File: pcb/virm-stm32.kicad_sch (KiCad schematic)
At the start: 25 parts, among them J1 Conn_02x10, J2 Conn_01x04, J3 TYPE-C-31-M-12, SW1 SW_SPDT, SW2 SW_Push, SW3 SW_Push, SW4 SW_Push, U1 STM32F070CBTx, U2 XC6206P332MR, Y1 16MHz

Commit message: Added footprint for usb port
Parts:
- J3: footprint (none) -> LCSC:TYPE-C-31-M-12
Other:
- note added: "Check if SCA/SCL is not inverted"
- note added: "Maybe add battery and regulator to wear it"
- note added: "TODO check pins for tristate capabilities"
- note added: "TODO: check footprint assigned pins"
- note removed: "SCA/SCL"
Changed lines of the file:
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@@
 	)
 	(junction
-		(at 77.47 111.76)
+		(at 50.8 175.26)
 		(diameter 0)
 		(color 0 0 0 0)
 	)
 	(junction
-		(at 50.8 175.26)
+		(at 74.93 35.56)
 		(diameter 0)
 		(color 0 0 0 0)
 	)
 	(junction
-		(at 74.93 35.56)
+		(at 59.69 160.02)
 		(diameter 0)
 		(color 0 0 0 0)
 	)
 	(junction
-		(at 59.69 160.02)
+		(at 36.83 116.84)
 		(diameter 0)
 		(color 0 0 0 0)
@@
 	)
 	(junction
+		(at 74.93 111.76)
+		(diameter 0)
+		(color 0 0 0 0)
+	)
+	(junction
 		(at 36.83 45.72)
 		(diameter 0)
@@
 	)
 	(junction
-		(at 41.91 116.84)
-		(diameter 0)
-		(color 0 0 0 0)
-	)
-	(junction
 		(at 87.63 45.72)
 		(diameter 0)
@@
 	(wire
 		(pts
-			(xy 50.8 111.76) (xy 52.07 111.76)
+			(xy 45.72 111.76) (xy 52.07 111.76)
 		)
 		(stroke
@@
 	(wire
 		(pts
-			(xy 50.8 109.22) (xy 52.07 109.22)
+			(xy 45.72 109.22) (xy 52.07 109.22)
 		)
 		(stroke
@@
 	(wire
 		(pts
-			(xy 41.91 116.84) (xy 52.07 116.84)
-		)
-		(stroke
-			(width 0)
-			(type default)
-		)
-	)
-	(wire
-		(pts
 			(xy 238.76 130.81) (xy 241.3 130.81)
 		)
@@
 	(wire
 		(pts
-			(xy 41.91 116.84) (xy 41.91 123.19)
+			(xy 36.83 116.84) (xy 36.83 123.19)
 		)
 		(stroke
@@
 	(wire
 		(pts
-			(xy 50.8 104.14) (xy 52.07 104.14)
+			(xy 45.72 104.14) (xy 52.07 104.14)
 		)
 		(stroke
@@
 	(wire
 		(pts
-			(xy 64.77 111.76) (xy 77.47 111.76)
+			(xy 64.77 111.76) (xy 74.93 111.76)
 		)
 		(stroke
@@
 	(wire
 		(pts
-			(xy 41.91 106.68) (xy 52.07 106.68)
+			(xy 36.83 106.68) (xy 52.07 106.68)
 		)
 		(stroke
@@
 	(wire
 		(pts
-			(xy 77.47 101.6) (xy 77.47 111.76)
+			(xy 74.93 101.6) (xy 74.93 111.76)
 		)
 		(stroke
@@
 	(wire
 		(pts
-			(xy 64.77 101.6) (xy 77.47 101.6)
+			(xy 64.77 101.6) (xy 74.93 101.6)
 		)
 		(stroke
@@
 	(wire
 		(pts
-			(xy 41.91 106.68) (xy 41.91 116.84)
+			(xy 36.83 106.68) (xy 36.83 116.84)
 		)
 		(stroke
@@
 	(wire
 		(pts
-			(xy 50.8 119.38) (xy 52.07 119.38)
+			(xy 36.83 116.84) (xy 52.07 116.84)
+		)
+		(stroke
+			(width 0)
+			(type default)
+		)
+	)
+	(wire
+		(pts
+			(xy 45.72 119.38) (xy 52.07 119.38)
 		)
 		(stroke
@@
 	(wire
 		(pts
-			(xy 77.47 111.76) (xy 77.47 123.19)
+			(xy 74.93 111.76) (xy 74.93 123.19)
 		)
 		(stroke
@@
 	(wire
 		(pts
-			(xy 50.8 114.3) (xy 52.07 114.3)
+			(xy 45.72 114.3) (xy 52.07 114.3)
 		)
 		(stroke
@@
 	(wire
 		(pts
-			(xy 50.8 121.92) (xy 52.07 121.92)
+			(xy 45.72 121.92) (xy 52.07 121.92)
 		)
 		(stroke
@@
 		)
 	)
-	(text "SCA/SCL\n"
-		(exclude_from_sim yes)
-		(at 94.996 100.584 0)
+	(text "TODO check pins for tristate capabilities"
+		(exclude_from_sim no)
+		(at 152.4 49.784 0)
+		(effects
+			(font
+				(size 1.27 1.27)
+			)
+		)
+	)
+	(text "TODO: check footprint assigned pins"
+		(exclude_from_sim no)
+		(at 218.44 137.16 0)
+		(effects
+			(font
+				(size 1.27 1.27)
+			)
+		)
+	)
+	(text "Check if SCA/SCL is not inverted"
+		(exclude_from_sim no)
+		(at 34.29 106.426 0)
+		(effects
+			(font
+				(size 1.27 1.27)
+			)
+		)
+	)
+	(text "Maybe add battery and regulator to wear it"
+		(exclude_from_sim no)
+		(at 207.772 21.082 0)
 		(effects
 			(font
@@
 		)
 	)
+	(label "SCA"
+		(at 46.99 109.22 0)
+		(fields_autoplaced yes)
+		(effects
+			(font
+				(size 1.27 1.27)
+			)
+			(justify left bottom)
+		)
+	)
 	(label "BOOT0"
 		(at 85.09 60.96 0)
@@
 		)
 	)
+	(label "SCL"
+		(at 46.99 111.76 0)
+		(fields_autoplaced yes)
+		(effects
+			(font
+				(size 1.27 1.27)
+			)
+			(justify left bottom)
+		)
+	)
 	(global_label "LED4"
 		(shape input)
@@
 	(global_label "PB6"
 		(shape input)
-		(at 50.8 111.76 180)
+		(at 45.72 111.76 180)
 		(fields_autoplaced yes)
 		(effects
@@
 		)
 		(property "Intersheetrefs" "${INTERSHEET_REFS}"
-			(at 44.0653 111.76 0)
+			(at 38.9853 111.76 0)
 			(effects
 				(font
@@
 	(global_label "PB7"
 		(shape input)
-		(at 50.8 109.22 180)
+		(at 45.72 109.22 180)
 		(fields_autoplaced yes)
 		(effects
@@
 		)
 		(property "Intersheetrefs" "${INTERSHEET_REFS}"
-			(at 44.0653 109.22 0)
+			(at 38.9853 109.22 0)
 			(effects
 				(font
@@
 	(global_label "PB8"
 		(shape input)
-		(at 50.8 104.14 180)
+		(at 45.72 104.14 180)
 		(fields_autoplaced yes)
 		(effects
@@
 		)
 		(property "Intersheetrefs" "${INTERSHEET_REFS}"
-			(at 44.0653 104.14 0)
+			(at 38.9853 104.14 0)
 			(effects
 				(font
@@
 	(global_label "PB3"
 		(shape input)
-		(at 50.8 121.92 180)
+		(at 45.72 121.92 180)
 		(fields_autoplaced yes)
 		(effects
@@
 		)
 		(property "Intersheetrefs" "${INTERSHEET_REFS}"
-			(at 44.0653 121.92 0)
+			(at 38.9853 121.92 0)
 			(effects
 				(font
@@
 	(global_label "PB5"
 		(shape input)
-		(at 50.8 114.3 180)
+		(at 45.72 114.3 180)
 		(fields_autoplaced yes)
 		(effects
@@
 		)
 		(property "Intersheetrefs" "${INTERSHEET_REFS}"
-			(at 44.0653 114.3 0)
+			(at 38.9853 114.3 0)
 			(effects
 				(font
@@
 	(global_label "PB4"
 		(shape input)
-		(at 50.8 119.38 180)
+		(at 45.72 119.38 180)
 		(fields_autoplaced yes)
 		(effects
@@
 		)
 		(property "Intersheetrefs" "${INTERSHEET_REFS}"
-			(at 44.0653 119.38 0)
+			(at 38.9853 119.38 0)
 			(effects
 				(font
@@
 	(symbol
 		(lib_id "power:GND")
-		(at 41.91 123.19 0)
+		(at 36.83 123.19 0)
 		(unit 1)
 		(exclude_from_sim no)
@@
 		(fields_autoplaced yes)
 		(property "Reference" "#PWR02"
-			(at 41.91 129.54 0)
+			(at 36.83 129.54 0)
 			(effects
 				(font
@@
 		)
 		(property "Value" "GND"
-			(at 41.91 128.27 0)
+			(at 36.83 128.27 0)
 			(effects
 				(font
@@
 		)
 		(property "Footprint" ""
-			(at 41.91 123.19 0)
+			(at 36.83 123.19 0)
 			(effects
 				(font
@@
 		)
 		(property "Datasheet" ""
-			(at 41.91 123.19 0)
+			(at 36.83 123.19 0)
 			(effects
 				(font
@@
 		)
 		(property "Description" "Power symbol creates a global label with name \"GND\" , ground"
-			(at 41.91 123.19 0)
+			(at 36.83 123.19 0)
 			(effects
 				(font
@@
 	(symbol
 		(lib_id "power:GND")
-		(at 77.47 123.19 0)
+		(at 74.93 123.19 0)
 		(unit 1)
 		(exclude_from_sim no)
@@
 		(fields_autoplaced yes)
 		(property "Reference" "#PWR08"
-			(at 77.47 129.54 0)
+			(at 74.93 129.54 0)
 			(effects
 				(font
@@
 		)
 		(property "Value" "GND"
-			(at 77.47 128.27 0)
+			(at 74.93 128.27 0)
 			(effects
 				(font
@@
 		)
 		(property "Footprint" ""
-			(at 77.47 123.19 0)
+			(at 74.93 123.19 0)
 			(effects
 				(font
@@
 		)
 		(property "Datasheet" ""
-			(at 77.47 123.19 0)
+			(at 74.93 123.19 0)
 			(effects
 				(font
@@
 		)
 		(property "Description" "Power symbol creates a global label with name \"GND\" , ground"
-			(at 77.47 123.19 0)
+			(at 74.93 123.19 0)
 			(effects
 				(font
@@
 			)
 		)
-		(property "Footprint" ""
+		(property "Footprint" "LCSC:TYPE-C-31-M-12"
 			(at 204.47 148.59 0)
 			(effects

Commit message: Started working on PCB layout
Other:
- note added: "TODO add two more pins for 18 columns of 5 leds"
- note removed: "Check if SCA/SCL is not inverted"
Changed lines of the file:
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@@
 		)
 	)
-	(text "Check if SCA/SCL is not inverted"
+	(text "Maybe add battery and regulator to wear it"
 		(exclude_from_sim no)
-		(at 34.29 106.426 0)
+		(at 207.772 21.082 0)
 		(effects
 			(font
@@
 		)
 	)
-	(text "Maybe add battery and regulator to wear it"
+	(text "TODO add two more pins for 18 columns of 5 leds"
 		(exclude_from_sim no)
-		(at 207.772 21.082 0)
+		(at 172.466 73.66 0)
 		(effects
 			(font
@@
 		)
 	)
-	(label "SCA"
+	(label "SDA"
 		(at 46.99 109.22 0)
 		(fields_autoplaced yes)

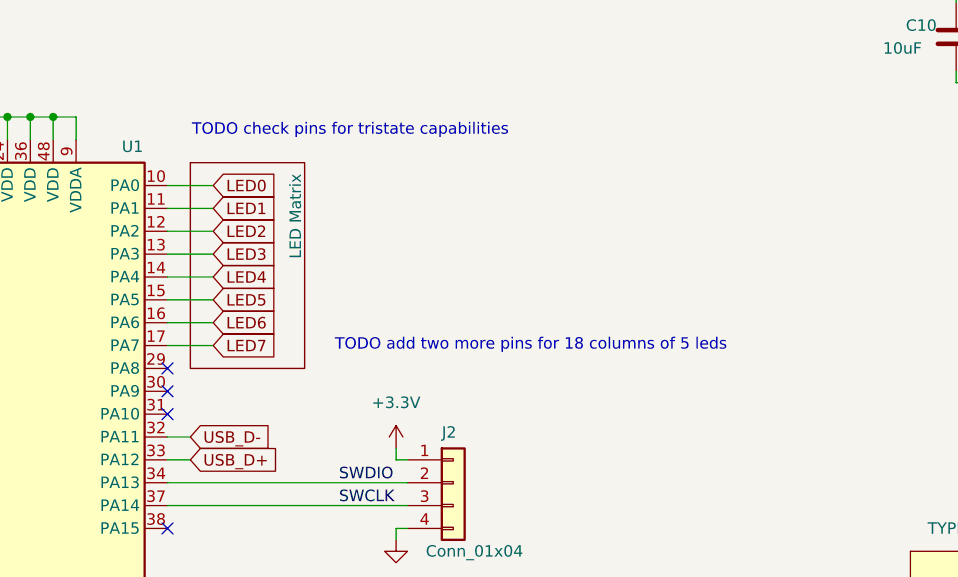
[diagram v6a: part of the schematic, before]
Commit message: started routing, with additional leds
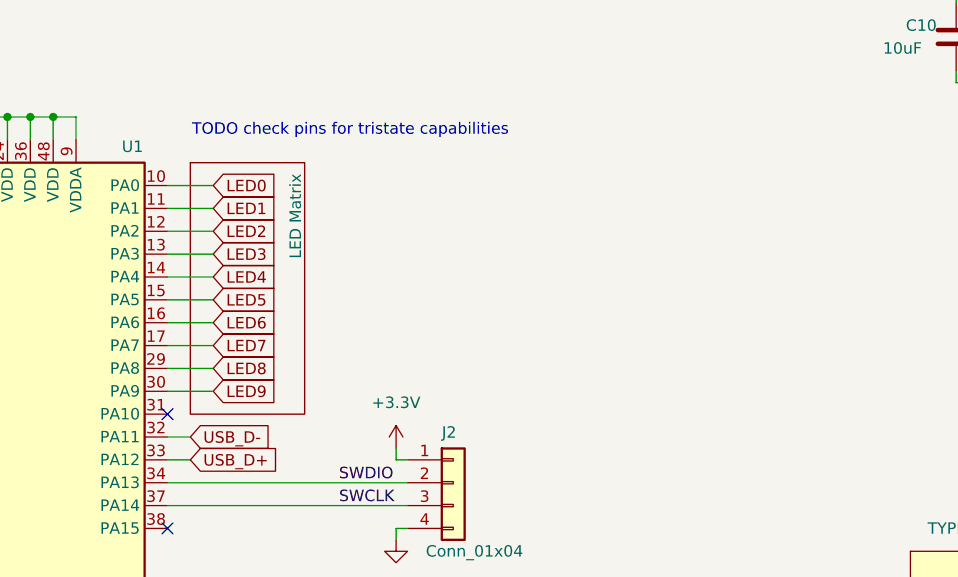
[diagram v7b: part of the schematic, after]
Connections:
- net LED8: now reaches U1.29 (PA8)
- net LED9: now reaches U1.30 (PA9)
- no-connect marks 14 -> 12
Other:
- note removed: "TODO add two more pins for 18 columns of 5 leds"
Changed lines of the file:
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@@
 	)
 	(no_connect
-		(at 132.08 78.74)
-	)
-	(no_connect
 		(at 238.76 107.95)
 	)
@@
 		(at 208.28 125.73)
 	)
-	(no_connect
-		(at 132.08 76.2)
-	)
 	(wire
 		(pts
@@
 	(wire
 		(pts
+			(xy 132.08 78.74) (xy 137.16 78.74)
+		)
+		(stroke
+			(width 0)
+			(type default)
+		)
+	)
+	(wire
+		(pts
 			(xy 137.16 55.88) (xy 132.08 55.88)
 		)
@@
 	(wire
 		(pts
+			(xy 132.08 76.2) (xy 137.16 76.2)
+		)
+		(stroke
+			(width 0)
+			(type default)
+		)
+	)
+	(wire
+		(pts
 			(xy 50.8 167.64) (xy 50.8 175.26)
 		)
@@
 		)
 	)
-	(text "TODO add two more pins for 18 columns of 5 leds"
-		(exclude_from_sim no)
-		(at 172.466 73.66 0)
-		(effects
-			(font
-				(size 1.27 1.27)
-			)
-		)
-	)
 	(label "SWCLK"
 		(at 151.13 91.44 0)
@@
 		)
 	)
+	(global_label "LED8"
+		(shape input)
+		(at 137.16 76.2 0)
+		(fields_autoplaced yes)
+		(effects
+			(font
+				(size 1.27 1.27)
+			)
+			(justify left)
+		)
+		(property "Intersheetrefs" "${INTERSHEET_REFS}"
+			(at 144.8018 76.2 0)
+			(effects
+				(font
+					(size 1.27 1.27)
+				)
+				(justify left)
+				(hide yes)
+			)
+		)
+	)
 	(global_label "PB8"
 		(shape input)
@@
 		)
 	)
+	(global_label "LED9"
+		(shape input)
+		(at 137.16 78.74 0)
+		(fields_autoplaced yes)
+		(effects
+			(font
+				(size 1.27 1.27)
+			)
+			(justify left)
+		)
+		(property "Intersheetrefs" "${INTERSHEET_REFS}"
+			(at 144.8018 78.74 0)
+			(effects
+				(font
+					(size 1.27 1.27)
+				)
+				(justify left)
+				(hide yes)
+			)
+		)
+	)
 	(global_label "LED6"
 		(shape input)
@@
 	(sheet
 		(at 134.62 53.34)
-		(size 12.7 22.86)
+		(size 12.7 27.94)
 		(stroke
 			(width 0.1524)

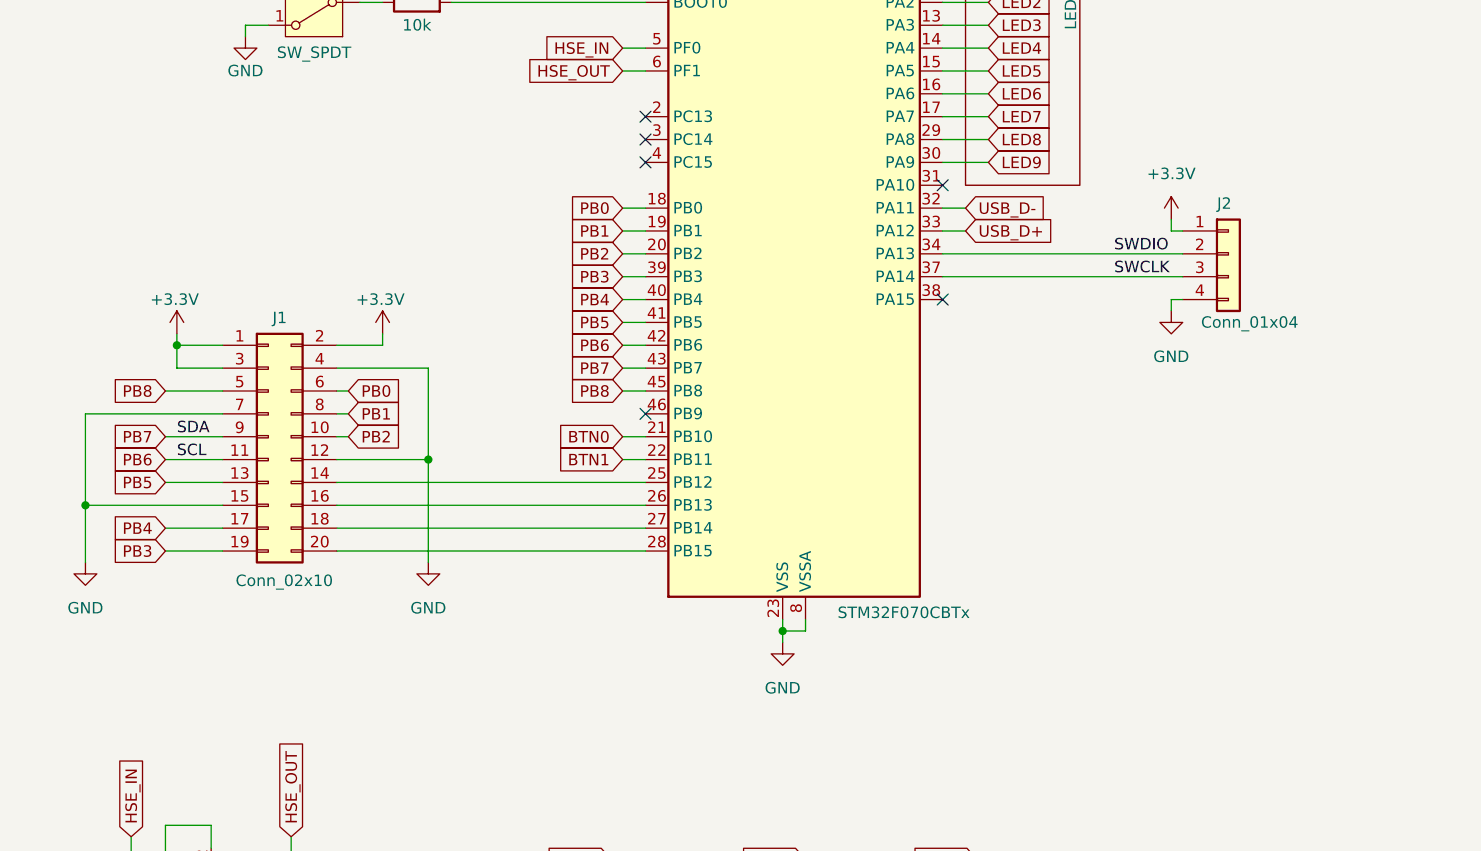
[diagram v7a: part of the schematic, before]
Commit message: First attempt at routing, also move the serial wire debug to the same header as the other IO's
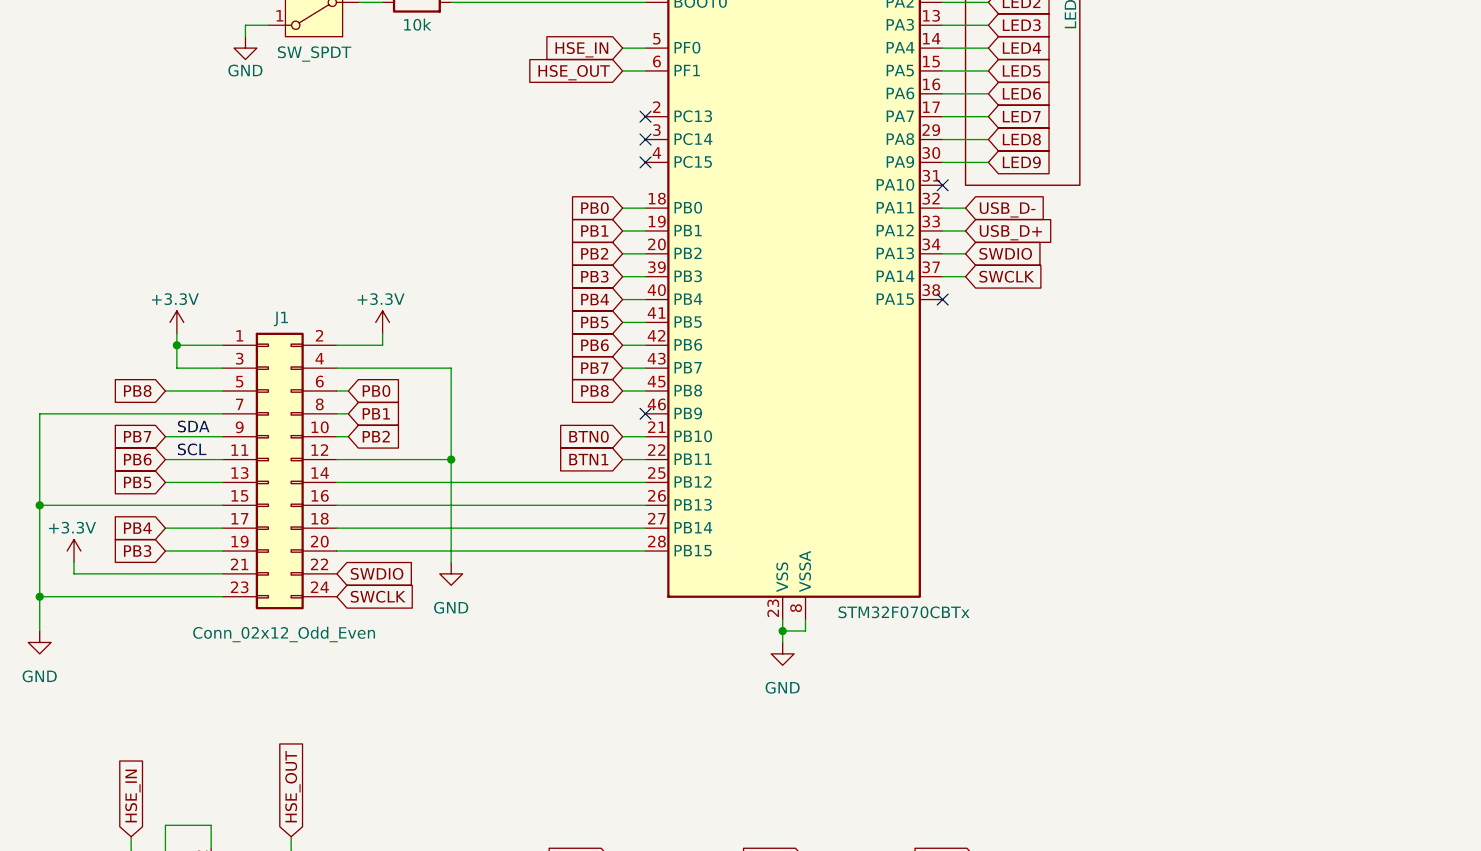
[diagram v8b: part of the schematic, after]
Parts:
- removed J1: Conn_02x10, Connector_PinHeader_2.54mm:PinHeader_2x10_P2.54mm_Vertical, symbol Connector_Generic:Conn_02x10_Odd_Even
- removed J2: Conn_01x04, Connector_PinSocket_2.54mm:PinSocket_1x04_P2.54mm_Vertical, symbol Connector_Generic:Conn_01x04
- added J1: Conn_02x12_Odd_Even, Connector_PinHeader_2.54mm:PinHeader_2x12_P2.54mm_Vertical, symbol Connector_Generic:Conn_02x12_Odd_Even
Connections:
- net +3.3V: now also J1.1 (Pin_1), J1.2 (Pin_2), J1.21 (Pin_21), J1.3 (Pin_3)
- net GND: now also J1.12 (Pin_12), J1.15 (Pin_15), J1.23 (Pin_23), J1.4 (Pin_4), J1.7 (Pin_7)
- net PB0: now also J1.6 (Pin_6)
- net PB1: now also J1.8 (Pin_8)
- net PB2: now also J1.10 (Pin_10)
- net PB3: now also J1.19 (Pin_19)
- net PB4: now also J1.17 (Pin_17)
- net PB5: now also J1.13 (Pin_13)
- net PB6: now also J1.11 (Pin_11)
- net PB7: now also J1.9 (Pin_9)
- net PB8: now also J1.5 (Pin_5)
- net SWCLK: now also J1.24 (Pin_24)
- net SWDIO: now also J1.22 (Pin_22)
- net at U1.25 (PB12): now also J1.14 (Pin_14)
- net at U1.26 (PB13): now also J1.16 (Pin_16)
- net at U1.27 (PB14): now also J1.18 (Pin_18)
- net at U1.28 (PB15): now also J1.20 (Pin_20)
